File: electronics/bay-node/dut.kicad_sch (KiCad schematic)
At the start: 24 parts, among them J5 AUX, Q2 2N7002, Q3 2N7002, U10 INA226AIDGSR, U9 TPS2553DDBVR

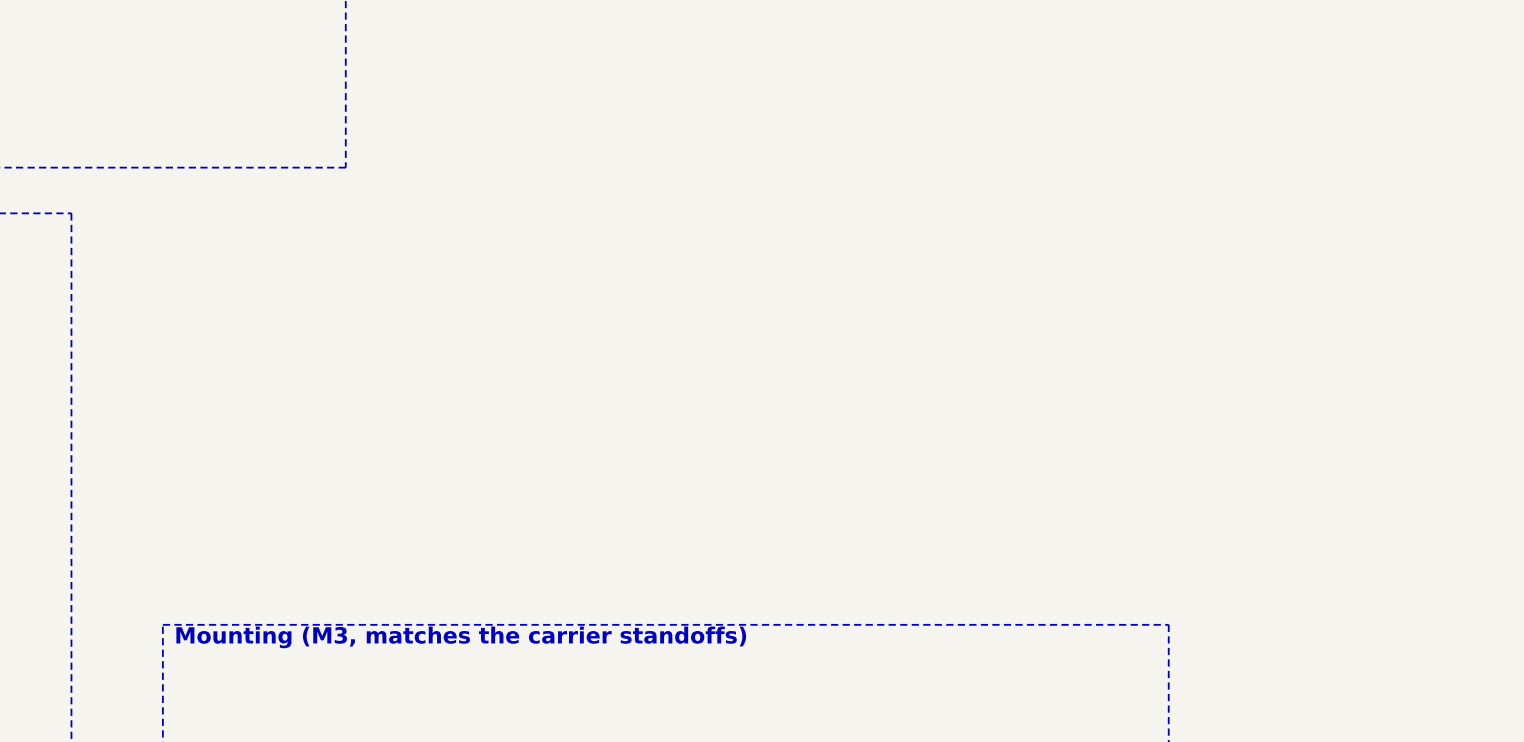
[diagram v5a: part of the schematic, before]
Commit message: Boards: labelled bottom test pads; hub dVdT 100 nF, 50 ms FLT blank
Eve's DFT rule on the four boards this session owns: bare pads on the
bottom, named on B.SilkS, out of the BOM and the CPL (no part, no
assembly fee).  Supply pads 1.5 mm, signal pads 1.0 mm (new catalog
entry "testpad1"), all more than 2 mm from any THT pad or hole
(closest: 4.7 mm, the pod's TP4).  Positions are fixed in design.py,
so they stay put across revisions.

- bay node, 17: TX, RX, 3V3, GND by the module (kept), then EN, IO0,
  FLT (DUT_FLT_N), ALRT (INA_ALERT_N), SDA, SCL and a second GND;
  a supply row along the bottom edge: GND, VIN, 5V, 3V3, DUT 5V,
  CAM 5V
- power hub, 20: TX, RX, 3V3, GND, 5V, VRACK, GND (kept), then EN,
  IO0, the CH224A's PD SDA/SCL, each row's FLT and IMON (A-D) and a
  third GND in the middle
- camera pod, 4: GND, 5V, 3V3 and a second GND at the far end
- DATA port, 2: GND and 5V (VBUS, through a via under its track)

Hub, as the datasheet audit's U1 answer asks (TPS2660 Fig. 55 at
85 C: 8-10 ms at 21 W fails the 47 nF worst start, 33 ms at 14 W
covers 100 nF): C21-C24 dVdT 47 nF -> 100 nF, so a row's soft start
is 16-22 ms and dissipates about 7-9 W typical, 14 W worst, for
19-24 ms; the firmware's HUB_ROW_FLT_BLANK_MS goes 25 -> 50 ms to
cover it (worst case 39 ms).  docs/power.md, the audit row and the
hub notes say so.

Routing fallout: J1's A12/B1 GND now leaves through one drawn 0.5 mm
via so the automatic fan-out can't cut the VRACK pour off A9/B4; the
pod's LDO tab zones are exclusive so tracks no longer split them.

All four rerouted, tidied and checked: ERC 0, DRC 0, unconnected 0,
parity 0.  Gerbers, renders, schematics, viewer GLBs, the JLC
snapshot lines and the rack BOM regenerated.

Co-Authored-By: Claude Opus 5.5 <noreply@anthropic.com>
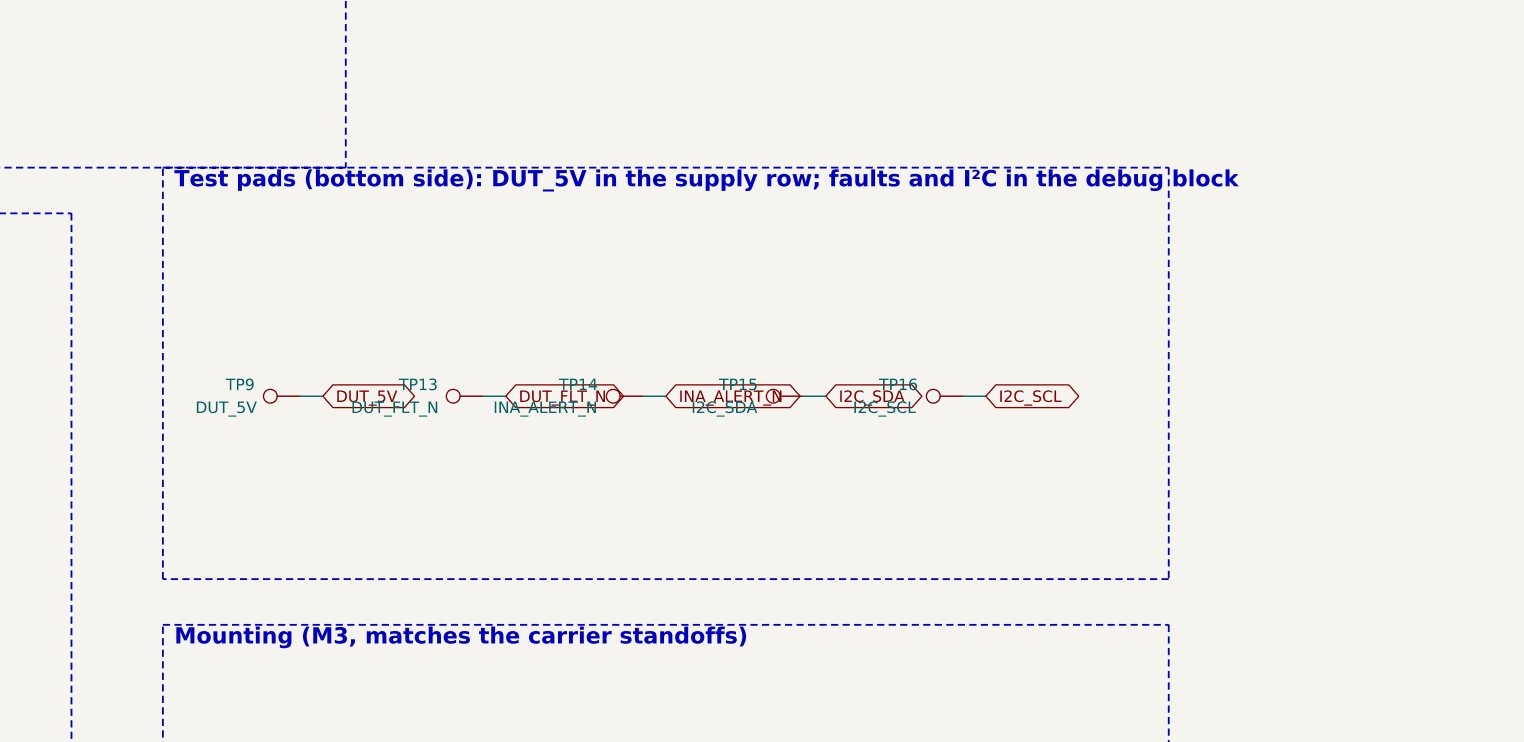
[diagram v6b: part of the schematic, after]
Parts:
- added TP13: DUT_FLT_N, TestPoint:TestPoint_Pad_D1.0mm, symbol Connector:TestPoint
- added TP14: INA_ALERT_N, TestPoint:TestPoint_Pad_D1.0mm, symbol Connector:TestPoint
- added TP15: I2C_SDA, TestPoint:TestPoint_Pad_D1.0mm, symbol Connector:TestPoint
- added TP16: I2C_SCL, TestPoint:TestPoint_Pad_D1.0mm, symbol Connector:TestPoint
- added TP9: DUT_5V, TestPoint:TestPoint_Pad_D1.5mm, symbol Connector:TestPoint
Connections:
- net DUT_5V: now also TP9.1
- net DUT_FLT_N: now also TP13.1
- net I2C_SCL: now also TP16.1
- net I2C_SDA: now also TP15.1
- net INA_ALERT_N: now also TP14.1
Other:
- note added: "Test pads (bottom side): DUT_5V in the supply row; faults and I²C in the debug block"

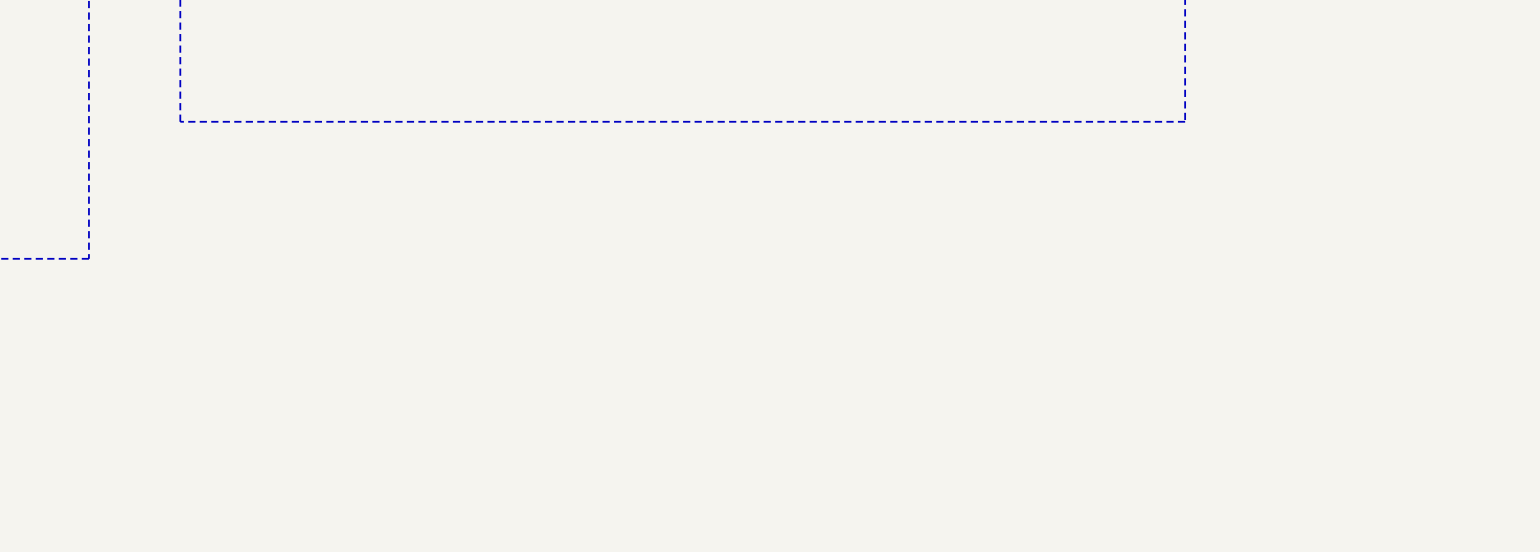
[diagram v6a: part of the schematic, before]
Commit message: Bay node: 15 more labelled bottom test pads (BN-2)
The kicad-happy review's BN-2, against Eve's rule: no pad on the camera
SPI, CAN TXD/RXD, POS_IN/POS_OUT, or the DUT's UART1 and RESET/BOOT, and
all three GND pads in the x 43-46 column.  TP18-TP32 are bare pads on
B.Cu, named on B.SilkS and kept out of the BOM and the CPL.  The
signals are 1.0 mm and each group's GND 1.5 mm:
- the camera SPI by R31-R34, on the lead side of the 33 ohm resistors:
  SCK, MOSI, MISO, CS, GND;
- by U11: CAN TXD, RXD, POS IN, GND;
- by the AUX column: AUX TX, AUX RX, RST, BOOT, POS OUT, GND.

Each pad sits where its net already runs, so no routing moves:
- 8 on a new via drawn on one of the net's F.Cu tracks (the three GNDs
  in the pours);
- 7 on one of the net's B.Cu tracks.
None adds a via on In2's VRACK strip.  All pads are at least 2 mm
from any through-hole pad or hole and 2.6 mm from each other, and no
B.SilkS label overlaps another.  The schematic gets a test pad frame
on each of the Camera, Rack bus and DUT power & AUX sheets.

pcbgen.fanout_pads now leaves alone a pad that holds a drawn via of
its own net (a test pad on its own via).  Fanning it out was
redundant, and in an incremental route the fan-out vias landed on
other nets' tracks.  On the hub, the next regeneration drops TP38's
GND fan-out (1.1 mm and a via); nothing else changes there.

Every track and via is main's, plus one 3 mm CAN_TXD stub that the
router laid over the existing track to reach the new via.  ERC 0,
DRC 0, unconnected 0, parity 0.

Co-Authored-By: Claude Opus 5.5 <noreply@anthropic.com>
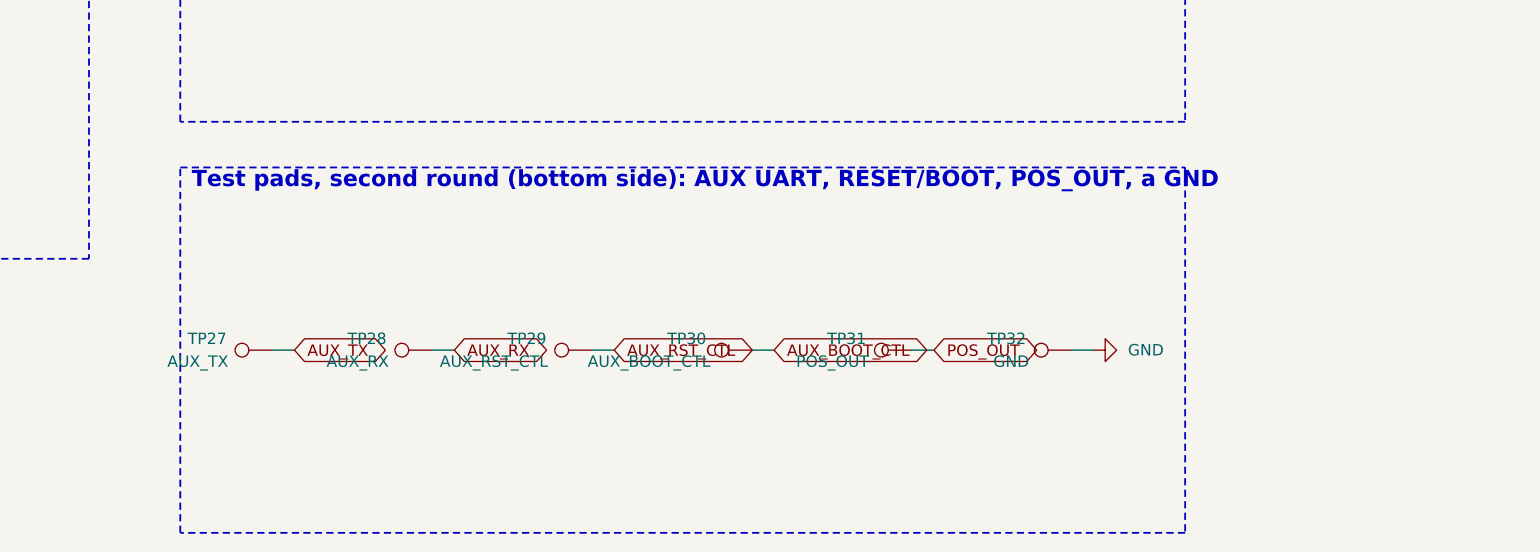
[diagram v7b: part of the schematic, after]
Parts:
- added TP27: AUX_TX, TestPoint:TestPoint_Pad_D1.0mm, symbol Connector:TestPoint
- added TP28: AUX_RX, TestPoint:TestPoint_Pad_D1.0mm, symbol Connector:TestPoint
- added TP29: AUX_RST_CTL, TestPoint:TestPoint_Pad_D1.0mm, symbol Connector:TestPoint
- added TP30: AUX_BOOT_CTL, TestPoint:TestPoint_Pad_D1.0mm, symbol Connector:TestPoint
- added TP31: POS_OUT, TestPoint:TestPoint_Pad_D1.0mm, symbol Connector:TestPoint
- added TP32: GND, TestPoint:TestPoint_Pad_D1.5mm, symbol Connector:TestPoint
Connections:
- net AUX_BOOT_CTL: now also TP30.1
- net AUX_RST_CTL: now also TP29.1
- net AUX_RX: now also TP28.1
- net AUX_TX: now also TP27.1
- net GND: now also TP32.1
- new net POS_OUT: TP31.1
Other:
- note added: "Test pads, second round (bottom side): AUX UART, RESET/BOOT, POS_OUT, a GND"
